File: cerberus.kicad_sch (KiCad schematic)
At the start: 5 parts

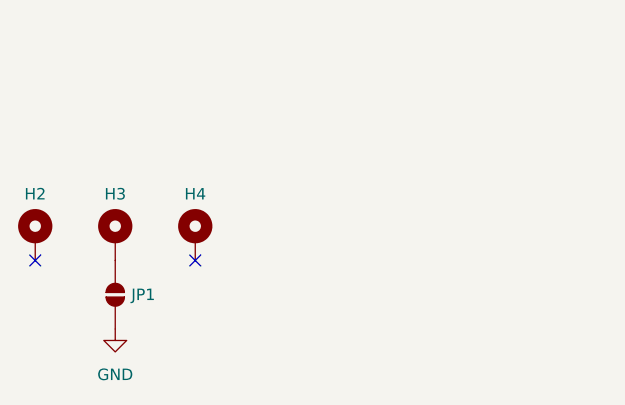
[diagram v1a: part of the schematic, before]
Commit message: Add fiducials and minor touchup
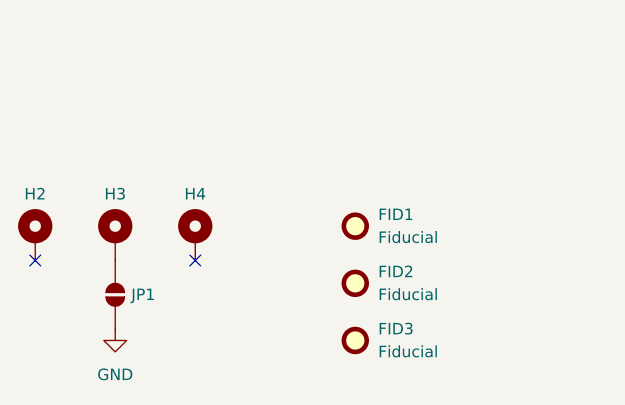
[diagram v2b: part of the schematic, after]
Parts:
- added FID1, FID2, FID3: Fiducial, Fiducial:Fiducial_1mm_Mask2mm, symbol Mechanical:Fiducial
